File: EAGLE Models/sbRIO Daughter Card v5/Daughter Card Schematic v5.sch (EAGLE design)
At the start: 71 parts, among them IC1 BTS716G, IC2 BTS716G, IC3 BTS716G, Q7 MMBT4403-7-F, Q8 MMBT4403-7-F, U2 ADXL345, U3 L3G4200D, X1 5566-2

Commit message: indermediate commit during layout
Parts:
- removed F19: 1A PTC, resistor:R-EU_R0603
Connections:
- new net N$1: TUB_CONN-3.KL
- new net N$2: TUB_CONN-1.KL
- net 12V: no longer F19.1
- net AI11: no longer AIO_PO_CONN-4.KL
- net AI15: no longer AIO_PO_CONN-8.KL
- net BSPD_OK_IN: now also R4.1, U$7.3~16V_IN; no longer R2.1, U$5.3~16V_IN
- net E-STOP_OK: now also AIO_PO_CONN-4.KL
- net GND: no longer AIO_PO_CONN-1.KL
- net IMD_OK_IN: now also R2.1, U$5.3~16V_IN; no longer R5.1, U$1.3~16V_IN
- net LATCH_OK: now also AIO_PO_CONN-8.KL, R5.1, U$1.3~16V_IN; no longer R4.1, U$7.3~16V_IN
- net N$29: no longer F19.2
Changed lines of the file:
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@@
 <part name="R16" library="resistor" deviceset="R-US_" device="R0402" value="4.7k"/>
 <part name="ACCUMULATOR_CONN" library="con-tycoelectronics" deviceset="RJ45*2" device="1-S" technology="-6L"/>
-<part name="F19" library="resistor" deviceset="R-EU_" device="R0603" value="1A PTC"/>
 <part name="AIO_PO_CONN" library="con-3m" deviceset="2516-" device="5"/>
 <part name="F15" library="resistor" deviceset="R-EU_" device="R0402" value="0.01A PTC"/>
@@
 <instance part="R16" gate="G$1" x="170.18" y="-63.5"/>
 <instance part="ACCUMULATOR_CONN" gate="G$1" x="469.9" y="-152.4"/>
-<instance part="F19" gate="G$1" x="454.66" y="-99.06"/>
 <instance part="AIO_PO_CONN" gate="-1" x="467.36" y="-104.14" rot="R180"/>
 <instance part="AIO_PO_CONN" gate="-2" x="467.36" y="-101.6" rot="R180"/>
@@
 </segment>
 <segment>
-<wire x1="419.1" y1="-104.14" x2="462.28" y2="-104.14" width="0.1524" layer="91"/>
-<label x="419.1" y="-104.14" size="1.778" layer="95" rot="R180" xref="yes"/>
-<pinref part="AIO_PO_CONN" gate="-1" pin="KL"/>
-</segment>
-<segment>
 <pinref part="R13" gate="G$1" pin="1"/>
 <wire x1="5.08" y1="-17.78" x2="5.08" y2="-22.86" width="0.1524" layer="91"/>
@@
 <label x="55.88" y="111.76" size="1.778" layer="95" rot="R90" xref="yes"/>
 <label x="5.08" y="30.48" size="1.778" layer="95" xref="yes"/>
-</segment>
-<segment>
-<pinref part="F19" gate="G$1" pin="1"/>
-<wire x1="449.58" y1="-99.06" x2="436.88" y2="-99.06" width="0.1524" layer="91"/>
-<label x="436.88" y="-99.06" size="1.778" layer="95" rot="R180" xref="yes"/>
 </segment>
 <segment>
@@
 <label x="467.36" y="43.18" size="1.778" layer="95" rot="R180" xref="yes"/>
 </segment>
-<segment>
-<wire x1="424.18" y1="-96.52" x2="462.28" y2="-96.52" width="0.1524" layer="91"/>
-<label x="424.18" y="-96.52" size="1.778" layer="95" rot="R180" xref="yes"/>
-<pinref part="AIO_PO_CONN" gate="-4" pin="KL"/>
-</segment>
 </net>
 <net name="AI10" class="0">
@@
 </segment>
 <segment>
-<pinref part="U$5" gate="G$1" pin="3~16V_IN"/>
-<wire x1="203.2" y1="2.54" x2="223.52" y2="2.54" width="0.1524" layer="91"/>
-<label x="223.52" y="2.54" size="1.778" layer="95" xref="yes"/>
-<pinref part="R2" gate="G$1" pin="1"/>
-<wire x1="203.2" y1="2.54" x2="203.2" y2="7.62" width="0.1524" layer="91"/>
-<junction x="203.2" y="7.62"/>
-<junction x="203.2" y="2.54"/>
+<pinref part="U$7" gate="G$1" pin="3~16V_IN"/>
+<wire x1="203.2" y1="27.94" x2="223.52" y2="27.94" width="0.1524" layer="91"/>
+<label x="223.52" y="27.94" size="1.778" layer="95" xref="yes"/>
+<pinref part="R4" gate="G$1" pin="1"/>
+<wire x1="203.2" y1="27.94" x2="203.2" y2="33.02" width="0.1524" layer="91"/>
+<junction x="203.2" y="33.02"/>
+<junction x="203.2" y="27.94"/>
 </segment>
 </net>
@@
 <label x="467.36" y="33.02" size="1.778" layer="95" rot="R180" xref="yes"/>
 </segment>
-<segment>
-<wire x1="462.28" y1="-86.36" x2="424.18" y2="-86.36" width="0.1524" layer="91"/>
-<label x="424.18" y="-86.36" size="1.778" layer="95" rot="R180" xref="yes"/>
-<pinref part="AIO_PO_CONN" gate="-8" pin="KL"/>
-</segment>
 </net>
 <net name="AO0" class="0">
@@
 </segment>
 <segment>
-<pinref part="U$1" gate="G$1" pin="3~16V_IN"/>
-<wire x1="203.2" y1="-22.86" x2="223.52" y2="-22.86" width="0.1524" layer="91"/>
-<label x="223.52" y="-22.86" size="1.778" layer="95" xref="yes"/>
-<pinref part="R5" gate="G$1" pin="1"/>
-<wire x1="203.2" y1="-22.86" x2="203.2" y2="-17.78" width="0.1524" layer="91"/>
-<junction x="203.2" y="-22.86"/>
-<junction x="203.2" y="-17.78"/>
+<pinref part="U$5" gate="G$1" pin="3~16V_IN"/>
+<wire x1="203.2" y1="2.54" x2="223.52" y2="2.54" width="0.1524" layer="91"/>
+<label x="223.52" y="2.54" size="1.778" layer="95" xref="yes"/>
+<pinref part="R2" gate="G$1" pin="1"/>
+<wire x1="203.2" y1="2.54" x2="203.2" y2="7.62" width="0.1524" layer="91"/>
+<junction x="203.2" y="7.62"/>
+<junction x="203.2" y="2.54"/>
 </segment>
 </net>
@@
 <net name="N$29" class="0">
 <segment>
-<pinref part="F19" gate="G$1" pin="2"/>
 <pinref part="AIO_PO_CONN" gate="-3" pin="KL"/>
 <wire x1="462.28" y1="-99.06" x2="459.74" y2="-99.06" width="0.1524" layer="91"/>
@@
 <junction x="203.2" y="20.32"/>
 </segment>
+<segment>
+<wire x1="424.18" y1="-96.52" x2="462.28" y2="-96.52" width="0.1524" layer="91"/>
+<label x="424.18" y="-96.52" size="1.778" layer="95" rot="R180" xref="yes"/>
+<pinref part="AIO_PO_CONN" gate="-4" pin="KL"/>
+</segment>
 </net>
 <net name="LATCH_OK" class="0">
 <segment>
-<pinref part="U$7" gate="G$1" pin="3~16V_IN"/>
-<wire x1="203.2" y1="27.94" x2="223.52" y2="27.94" width="0.1524" layer="91"/>
-<label x="223.52" y="27.94" size="1.778" layer="95" xref="yes"/>
-<pinref part="R4" gate="G$1" pin="1"/>
-<wire x1="203.2" y1="27.94" x2="203.2" y2="33.02" width="0.1524" layer="91"/>
-<junction x="203.2" y="33.02"/>
-<junction x="203.2" y="27.94"/>
+<wire x1="462.28" y1="-86.36" x2="424.18" y2="-86.36" width="0.1524" layer="91"/>
+<label x="424.18" y="-86.36" size="1.778" layer="95" rot="R180" xref="yes"/>
+<pinref part="AIO_PO_CONN" gate="-8" pin="KL"/>
+</segment>
+<segment>
+<pinref part="U$1" gate="G$1" pin="3~16V_IN"/>
+<wire x1="203.2" y1="-22.86" x2="223.52" y2="-22.86" width="0.1524" layer="91"/>
+<label x="223.52" y="-22.86" size="1.778" layer="95" xref="yes"/>
+<pinref part="R5" gate="G$1" pin="1"/>
+<wire x1="203.2" y1="-22.86" x2="203.2" y2="-17.78" width="0.1524" layer="91"/>
+<junction x="203.2" y="-22.86"/>
+<junction x="203.2" y="-17.78"/>
 </segment>
 </net>
@@
 </segment>
 </net>
+<net name="N$1" class="0">
+<segment>
+<pinref part="TUB_CONN" gate="-3" pin="KL"/>
+<wire x1="462.28" y1="-35.56" x2="421.64" y2="-35.56" width="0.1524" layer="91"/>
+<label x="421.64" y="-35.56" size="1.778" layer="95" rot="R180" xref="yes"/>
+</segment>
+</net>
+<net name="N$2" class="0">
+<segment>
+<pinref part="TUB_CONN" gate="-1" pin="KL"/>
+<wire x1="462.28" y1="-40.64" x2="421.64" y2="-40.64" width="0.1524" layer="91"/>
+<label x="421.64" y="-40.64" size="1.778" layer="95" rot="R180" xref="yes"/>
+</segment>
+</net>

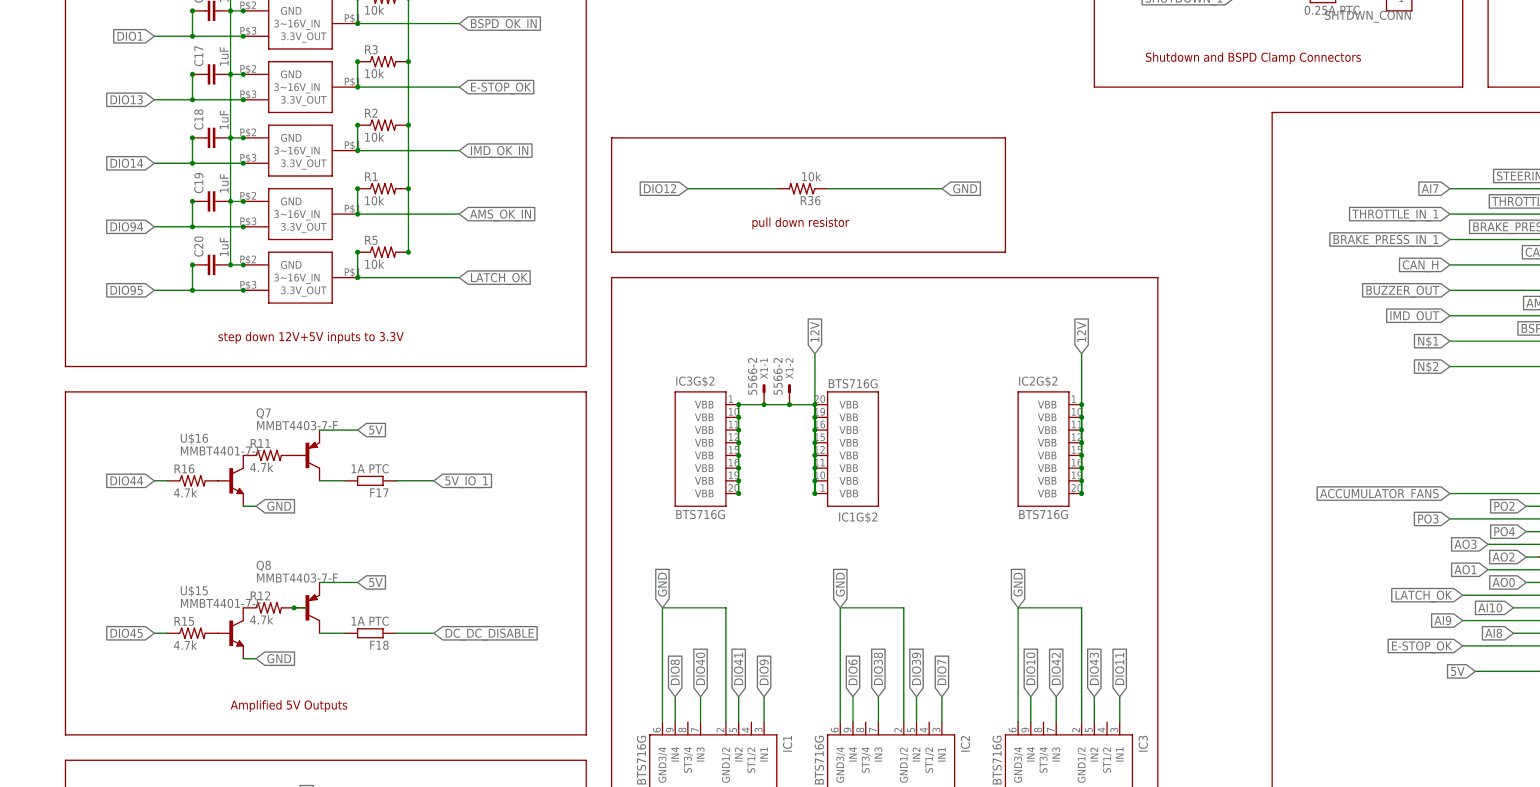
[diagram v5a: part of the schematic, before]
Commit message: Made board pass DRC
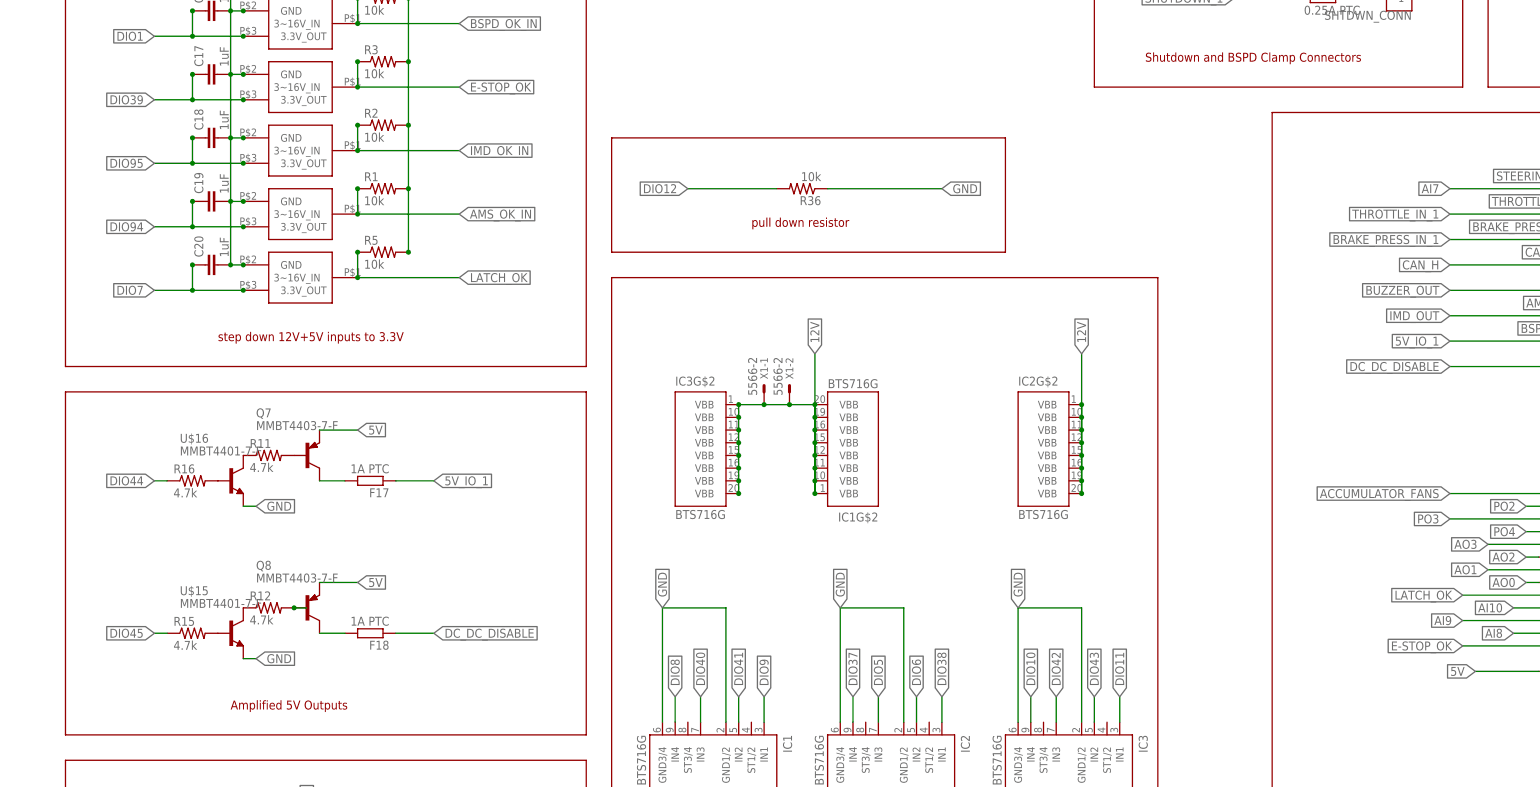
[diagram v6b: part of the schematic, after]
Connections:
- removed net N$1: TUB_CONN-3.KL
- removed net N$2: TUB_CONN-1.KL
- net 5V_IO_1: now also TUB_CONN-3.KL
- net DC_DC_DISABLE: now also TUB_CONN-1.KL
- net DIO13: no longer C17.1, U$6.3.3V_OUT
- net DIO14: no longer C18.1, U$5.3.3V_OUT
- net DIO37: now also IC2G$1.IN4
- net DIO38: now also IC2G$1.IN1; no longer IC2G$1.IN3
- net DIO39: now also C17.1, U$6.3.3V_OUT; no longer IC2G$1.IN2
- net DIO5: now also IC2G$1.IN3
- net DIO6: now also IC2G$1.IN2; no longer IC2G$1.IN4
- net DIO7: now also C20.1, U$1.3.3V_OUT; no longer IC2G$1.IN1
- net DIO95: now also C18.1, U$5.3.3V_OUT; no longer C20.1, U$1.3.3V_OUT
